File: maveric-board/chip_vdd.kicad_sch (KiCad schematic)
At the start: 17 parts, among them U1 Socket

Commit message: add fmc lpc symbol
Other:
- title: (none) -> Maveric Board
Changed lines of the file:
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@@
 	(paper "A3")
 	(title_block
-		(date "2024-06-09")
+		(title "Maveric Board")
+		(date "2024-06-10")
 		(rev "0")
+		(comment 1 "Drawn By: Vighnesh Iyer")
 	)
 	(junction

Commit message: add jlcpcb 10u cap part + footprint
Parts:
- C1, C10, C11, C12, C13, C14, C15, C16, C2, C3, C4, C5, C6, C7, C8, C9: footprint (none) -> Capacitor_SMD:C_0603_1608Metric; JLCPCB Part # (none) -> C95839

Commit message: reannotate, fix all ERCs
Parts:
- renumbered C3 to C1, C1 to C2, C2 to C3, U1 to U3

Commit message: add uni2 socket footprint, check against drawing, fix npth, assign all footprints and part numbers
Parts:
- U3: footprint (none) -> maveric-parts:BGA-1733-.92-47.725x47.725
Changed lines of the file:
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@@
 			)
 		)
-		(property "Footprint" ""
+		(property "Footprint" "maveric-parts:BGA-1733-.92-47.725x47.725"
 			(at 35.56 29.21 0)
 			(effects
@@
 			)
 		)
-		(property "Footprint" ""
+		(property "Footprint" "maveric-parts:BGA-1733-.92-47.725x47.725"
 			(at 128.27 30.48 0)
 			(effects
@@
 			)
 		)
-		(property "Footprint" ""
+		(property "Footprint" "maveric-parts:BGA-1733-.92-47.725x47.725"
 			(at 312.42 31.75 0)
 			(effects
@@
 			)
 		)
-		(property "Footprint" ""
+		(property "Footprint" "maveric-parts:BGA-1733-.92-47.725x47.725"
 			(at 219.71 31.75 0)
 			(effects

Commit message: add testpoint for pg_c2m and fixup footprints for led and mosfet with correct pin mapping
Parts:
- renumbered C1 to C11, C2 to C12, C3 to C13, C4 to C14, C5 to C15, C6 to C16, C7 to C17, C8 to C18, C9 to C19, C10 to C20, C11 to C21, C12 to C22, C13 to C23, C14 to C24, C15 to C25, C16 to C26

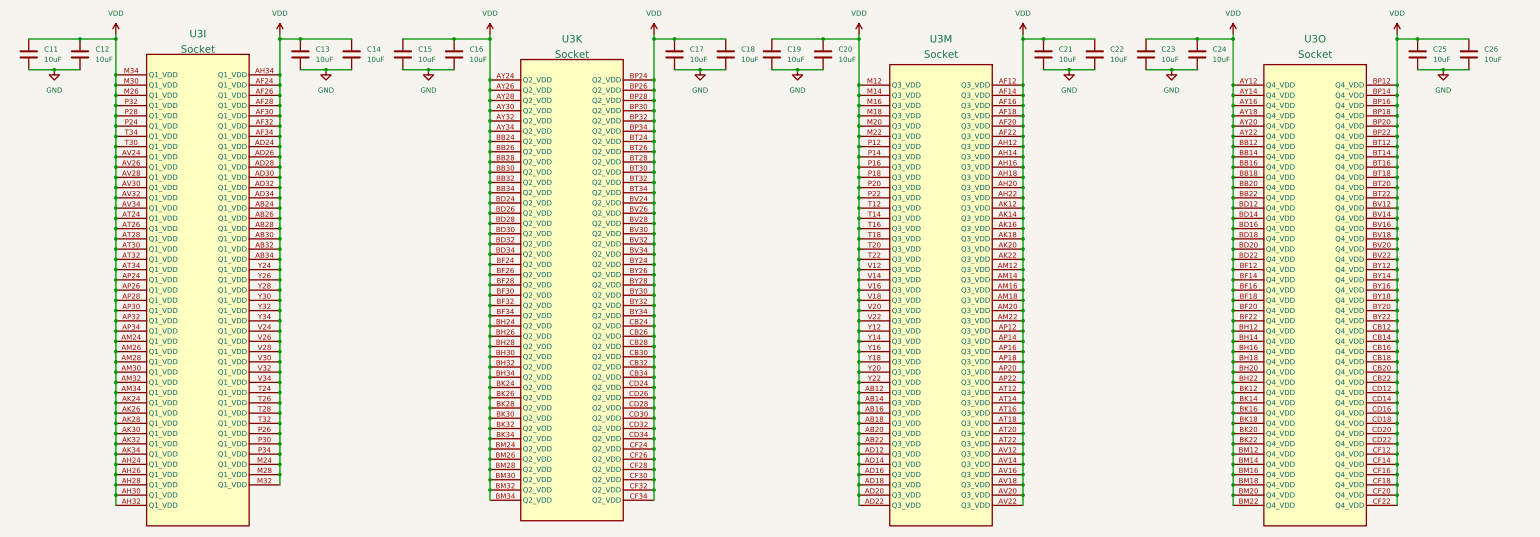
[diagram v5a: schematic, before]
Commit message: some docs + dnp uni2 socket
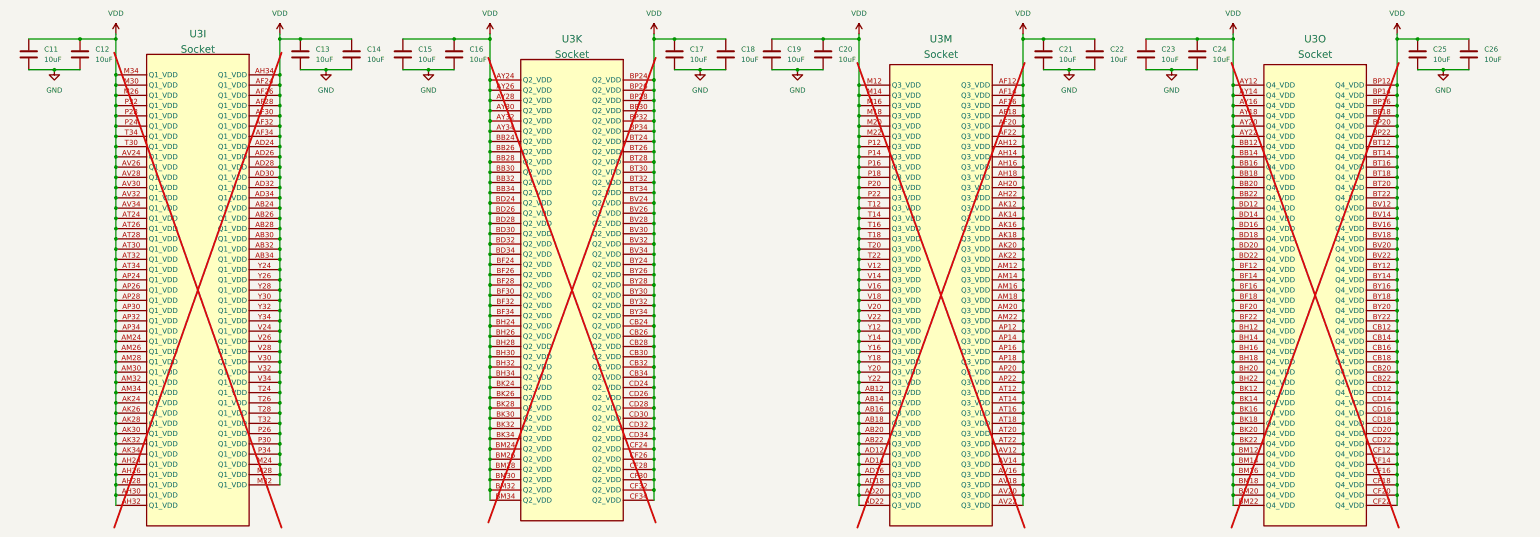
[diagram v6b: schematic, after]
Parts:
- U3: now not fitted
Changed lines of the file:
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@@
 		(in_bom yes)
 		(on_board yes)
-		(dnp no)
+		(dnp yes)
 		(fields_autoplaced yes)
 		(property "Reference" "U3"
@@
 		(in_bom yes)
 		(on_board yes)
-		(dnp no)
+		(dnp yes)
 		(fields_autoplaced yes)
 		(property "Reference" "U3"
@@
 		(in_bom yes)
 		(on_board yes)
-		(dnp no)
+		(dnp yes)
 		(fields_autoplaced yes)
 		(property "Reference" "U3"
@@
 		(in_bom yes)
 		(on_board yes)
-		(dnp no)
+		(dnp yes)
 		(fields_autoplaced yes)
 		(property "Reference" "U3"

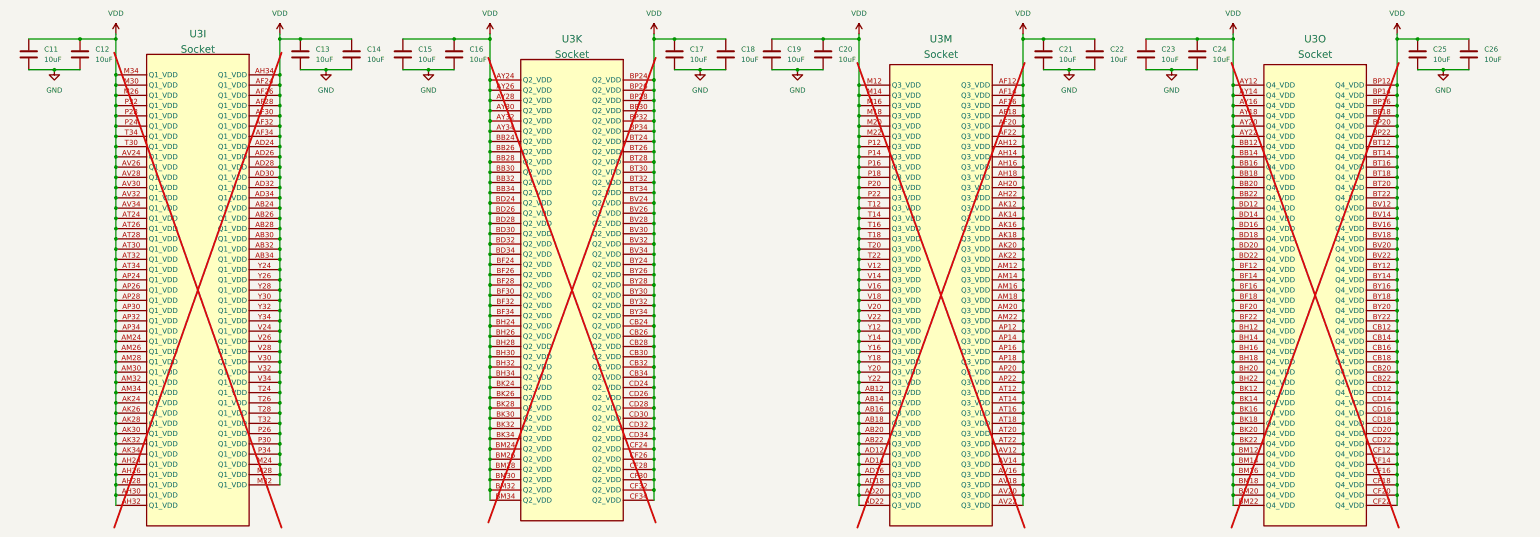
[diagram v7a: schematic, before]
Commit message: add mfr part # attribute to each symbol, resync board layout, remove excess VDDV decap
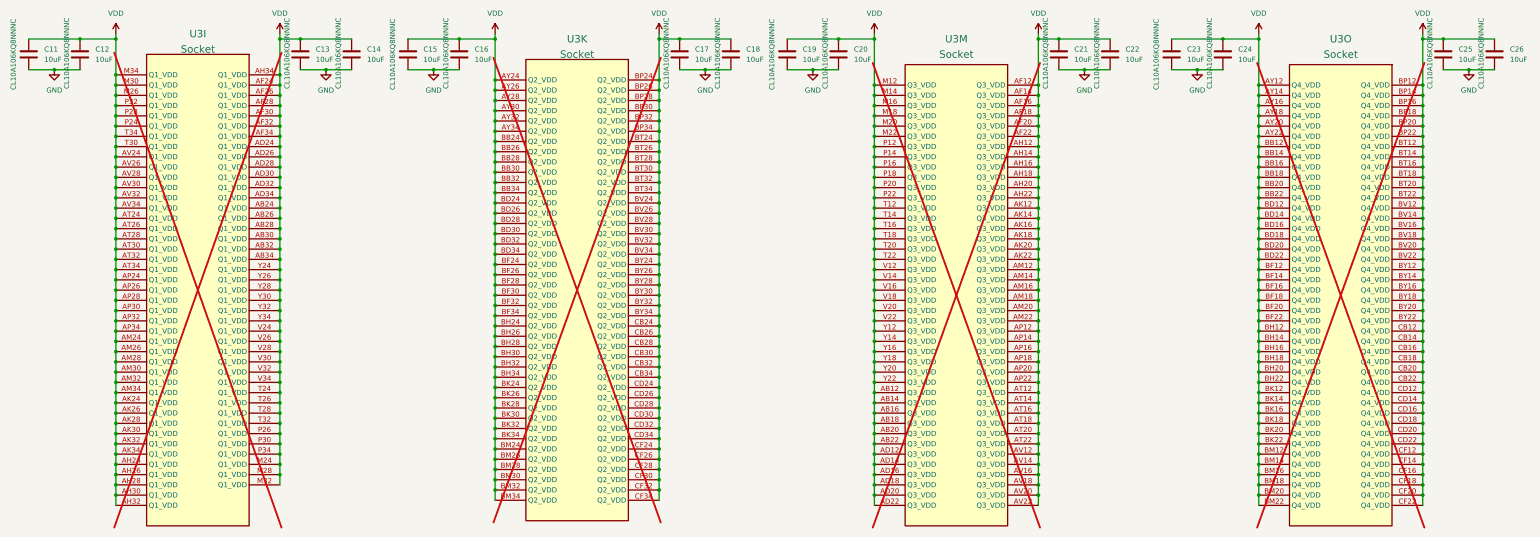
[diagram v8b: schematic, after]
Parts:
- C11, C12, C13, C14, C15, C16, C17, C18, C19, C20, C21, C22, C23, C24, C25, C26: Mfr Part # (none) -> CL10A106KQ8NNNC
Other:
- moved on the sheet: U3K, U3M, U3O
